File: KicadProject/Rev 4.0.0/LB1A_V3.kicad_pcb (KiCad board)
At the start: 6 copper layers, 42 x 42 mm, 187 parts, among them J601 2337019-1, J602 2337019-1, U101 STM32MP157CAA3, U201 AS4C256M16D3LC-12BCN, U401 STPMIC1xPQR, U501 S40FC004C1B2C00000, U601 LBEE59B1LV-278, U701 DF40C-70DP-0.4V(51), U702 DF40C-100DP-0.4V(51), U703 DF40C-100DP-0.4V(51), X101 32.768kHz, Y101 24MHz

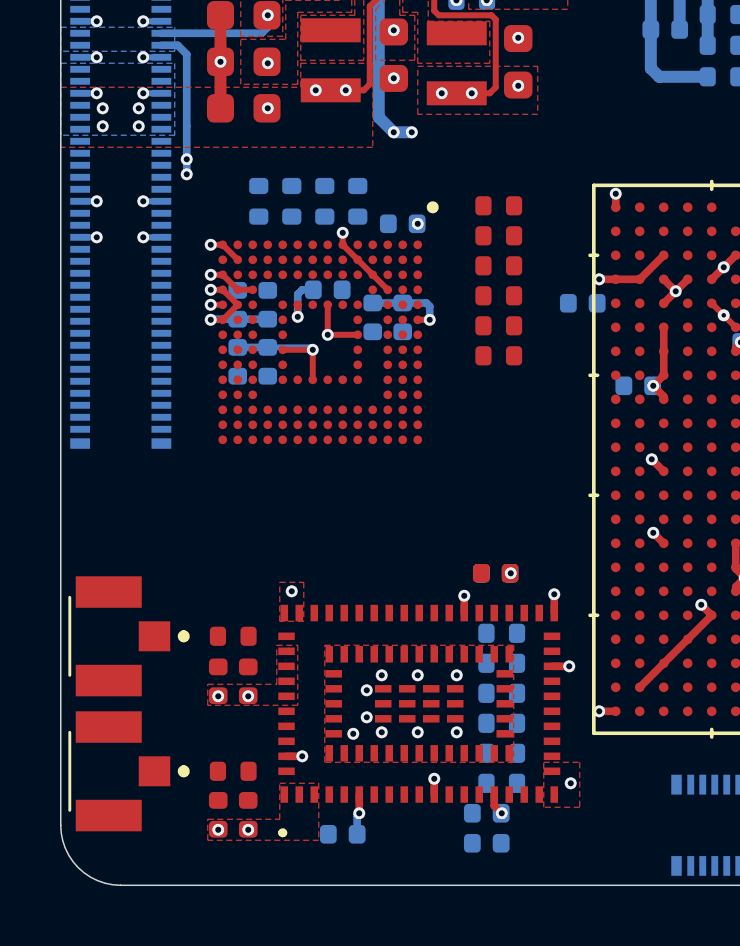
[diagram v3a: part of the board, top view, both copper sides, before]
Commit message: power planes complete.
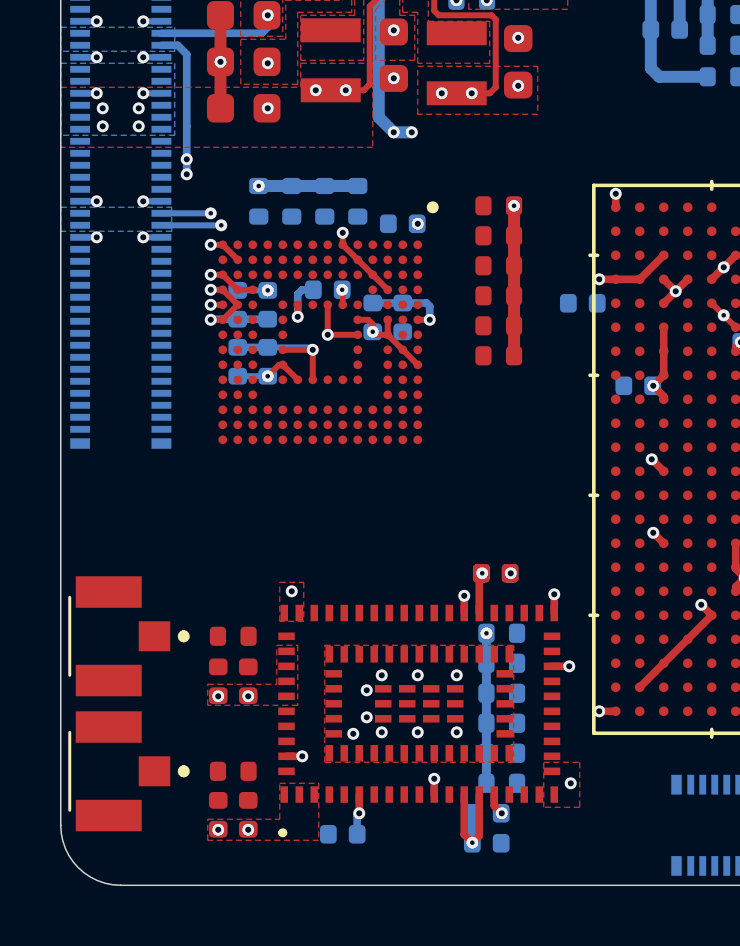
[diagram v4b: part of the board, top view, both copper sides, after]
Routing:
- net PMIC_LDO5_2V9: track 12.7 -> 31.8 mm, vias 5 -> 13
- net PMIC_LDO1_1V8: track 9.00 -> 19.8 mm, vias 3 -> 6
- added copper zone on B.Cu, net PMIC_LDO5_2V9
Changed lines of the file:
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@@
     (thickness 1.2)
     (drawings 8)
-    (tracks 814)
+    (tracks 871)
     (zones 0)
     (modules 187)
@@
   )
   (setup
-    (last_trace_width 0.2)
+    (last_trace_width 0.3)
     (user_trace_width 0.1)
     (user_trace_width 0.127)
@@
   (gr_arc (start 173 128) (end 171 128) (angle -90) (layer Edge.Cuts) (width 0.05))
   (gr_arc (start 173 90) (end 173 88) (angle -90) (layer Edge.Cuts) (width 0.05))
+  (via (at 185.05 119.6) (size 0.4) (drill 0.15) (layers L1_Sig_Pwr.Cu L6_Sig_Pwr.Cu) (net 21))
   (via (at 207.05 110) (size 0.4) (drill 0.15) (layers L1_Sig_Pwr.Cu L6_Sig_Pwr.Cu) (net 9))
   (via (at 201.2 97.4) (size 0.4) (drill 0.15) (layers L1_Sig_Pwr.Cu L6_Sig_Pwr.Cu) (net 9))
@@
   (via (at 175.2 106.3) (size 0.4) (drill 0.2) (layers L1_Sig_Pwr.Cu L6_Sig_Pwr.Cu) (net 21))
   (segment (start 175.2 105.8) (end 175.2 106.3) (width 0.254) (layer L6_Sig_Pwr.Cu) (net 21))
+  (segment (start 185.19 123.6) (end 185.19 123.6) (width 0.4) (layer L6_Sig_Pwr.Cu) (net 21))
+  (segment (start 185.19 123.6) (end 185.19 122.6) (width 0.3) (layer L6_Sig_Pwr.Cu) (net 21))
+  (segment (start 185.19 125.6) (end 185.19 124.6) (width 0.3) (layer L6_Sig_Pwr.Cu) (net 21))
+  (segment (start 185.19 124.6) (end 185.19 124.6) (width 0.4) (layer L6_Sig_Pwr.Cu) (net 21))
+  (segment (start 185.19 125.6) (end 185.19 126.6) (width 0.3) (layer L6_Sig_Pwr.Cu) (net 21))
+  (segment (start 184.72 127.6) (end 184.72 128.58) (width 0.3) (layer L6_Sig_Pwr.Cu) (net 21))
+  (segment (start 184.72 128.58) (end 184.72 128.6) (width 0.4) (layer L6_Sig_Pwr.Cu) (net 21))
+  (via (at 184.72 128.58) (size 0.4) (drill 0.15) (layers L1_Sig_Pwr.Cu L6_Sig_Pwr.Cu) (net 21))
+  (segment (start 184.45 128.31) (end 184.72 128.58) (width 0.254) (layer L1_Sig_Pwr.Cu) (net 21))
+  (segment (start 184.45 126.975) (end 184.45 128.31) (width 0.254) (layer L1_Sig_Pwr.Cu) (net 21))
+  (segment (start 184.95 128.35) (end 184.72 128.58) (width 0.254) (layer L1_Sig_Pwr.Cu) (net 21))
+  (segment (start 184.95 126.975) (end 184.95 128.35) (width 0.254) (layer L1_Sig_Pwr.Cu) (net 21))
+  (segment (start 184.95 119.7) (end 185.05 119.6) (width 0.254) (layer L1_Sig_Pwr.Cu) (net 21))
+  (segment (start 184.95 120.925) (end 184.95 119.7) (width 0.254) (layer L1_Sig_Pwr.Cu) (net 21))
+  (segment (start 185.19 122.6) (end 185.19 121.6) (width 0.3) (layer L6_Sig_Pwr.Cu) (net 21))
+  (segment (start 185.19 121.6) (end 185.19 121.6) (width 0.3) (layer L6_Sig_Pwr.Cu) (net 21))
+  (via (at 185.19 121.6) (size 0.4) (drill 0.15) (layers L1_Sig_Pwr.Cu L6_Sig_Pwr.Cu) (net 21))
+  (segment (start 185.19 124.6) (end 185.19 123.6) (width 0.3) (layer L6_Sig_Pwr.Cu) (net 21))
   (segment (start 177.875 99.45) (end 177.85 99.45) (width 0.254) (layer L1_Sig_Pwr.Cu) (net 22))
   (via (at 175.6 100.2) (size 0.4) (drill 0.2) (layers L1_Sig_Pwr.Cu L6_Sig_Pwr.Cu) (net 22))
@@
   (via (at 176 110.65) (size 0.4) (drill 0.2) (layers L1_Sig_Pwr.Cu L6_Sig_Pwr.Cu) (net 24))
   (segment (start 176.4 110.65) (end 176 110.65) (width 0.2) (layer L1_Sig_Pwr.Cu) (net 24))
+  (segment (start 186.11 112.35) (end 186.11 111.35) (width 0.4) (layer L1_Sig_Pwr.Cu) (net 24))
+  (segment (start 186.11 111.35) (end 186.11 110.35) (width 0.4) (layer L1_Sig_Pwr.Cu) (net 24))
+  (segment (start 186.11 110.35) (end 186.11 109.35) (width 0.4) (layer L1_Sig_Pwr.Cu) (net 24))
+  (segment (start 186.11 109.35) (end 186.11 108.35) (width 0.4) (layer L1_Sig_Pwr.Cu) (net 24))
+  (segment (start 186.11 108.35) (end 186.11 108.11) (width 0.4) (layer L1_Sig_Pwr.Cu) (net 24))
+  (segment (start 186.11 108.11) (end 186.11 107.35) (width 0.4) (layer L1_Sig_Pwr.Cu) (net 24))
+  (segment (start 186.11 107.35) (end 186.11 107.35) (width 0.4) (layer L1_Sig_Pwr.Cu) (net 24))
+  (via (at 186.11 107.35) (size 0.4) (drill 0.15) (layers L1_Sig_Pwr.Cu L6_Sig_Pwr.Cu) (net 24))
+  (segment (start 180.9 106.69) (end 179.8 106.69) (width 0.4) (layer L6_Sig_Pwr.Cu) (net 24))
+  (segment (start 179.8 106.69) (end 178.7 106.69) (width 0.4) (layer L6_Sig_Pwr.Cu) (net 24))
+  (segment (start 178.7 106.69) (end 177.6 106.69) (width 0.4) (layer L6_Sig_Pwr.Cu) (net 24))
+  (segment (start 177.6 106.69) (end 177.6 106.69) (width 0.4) (layer L6_Sig_Pwr.Cu) (net 24))
+  (via (at 177.6 106.69) (size 0.4) (drill 0.15) (layers L1_Sig_Pwr.Cu L6_Sig_Pwr.Cu) (net 24))
+  (via (at 180.38 110.15) (size 0.4) (drill 0.15) (layers L1_Sig_Pwr.Cu L6_Sig_Pwr.Cu) (net 24))
+  (segment (start 180.4 110.17) (end 180.38 110.15) (width 0.2) (layer L1_Sig_Pwr.Cu) (net 24))
+  (segment (start 180.4 110.65) (end 180.4 110.17) (width 0.2) (layer L1_Sig_Pwr.Cu) (net 24))
+  (segment (start 180.9 111.15) (end 181.25 111.15) (width 0.2) (layer L1_Sig_Pwr.Cu) (net 24))
+  (via (at 181.4 111.55) (size 0.4) (drill 0.15) (layers L1_Sig_Pwr.Cu L6_Sig_Pwr.Cu) (net 24))
+  (segment (start 181.4 111.3) (end 181.4 111.55) (width 0.2) (layer L1_Sig_Pwr.Cu) (net 24))
+  (segment (start 181.25 111.15) (end 181.4 111.3) (width 0.2) (layer L1_Sig_Pwr.Cu) (net 24))
+  (segment (start 181.9 111.15) (end 181.9 111.65) (width 0.2) (layer L1_Sig_Pwr.Cu) (net 24))
+  (segment (start 181.9 111.65) (end 182.4 112.15) (width 0.2) (layer L1_Sig_Pwr.Cu) (net 24))
+  (segment (start 182.4 112.15) (end 182.9 112.65) (width 0.2) (layer L1_Sig_Pwr.Cu) (net 24))
+  (segment (start 181.5 111.65) (end 181.4 111.55) (width 0.2) (layer L1_Sig_Pwr.Cu) (net 24))
+  (segment (start 181.9 111.65) (end 181.5 111.65) (width 0.2) (layer L1_Sig_Pwr.Cu) (net 24))
+  (segment (start 178.9 113.15) (end 178.4 112.65) (width 0.2) (layer L1_Sig_Pwr.Cu) (net 24))
+  (via (at 177.9 113.03) (size 0.4) (drill 0.15) (layers L1_Sig_Pwr.Cu L6_Sig_Pwr.Cu) (net 24))
+  (segment (start 178.28 112.65) (end 177.9 113.03) (width 0.2) (layer L1_Sig_Pwr.Cu) (net 24))
+  (segment (start 178.4 112.65) (end 178.28 112.65) (width 0.2) (layer L1_Sig_Pwr.Cu) (net 24))
+  (segment (start 176.9 113.03) (end 177.9 113.03) (width 0.2) (layer L6_Sig_Pwr.Cu) (net 24))
+  (segment (start 176.9 110.17) (end 177.9 110.17) (width 0.2) (layer L6_Sig_Pwr.Cu) (net 24))
+  (segment (start 177.9 110.17) (end 177.9 110.17) (width 0.2) (layer L6_Sig_Pwr.Cu) (net 24))
+  (via (at 177.9 110.17) (size 0.4) (drill 0.15) (layers L1_Sig_Pwr.Cu L6_Sig_Pwr.Cu) (net 24))
+  (via (at 176 107.6) (size 0.4) (drill 0.15) (layers L1_Sig_Pwr.Cu L6_Sig_Pwr.Cu) (net 24))
+  (segment (start 174.355 107.6) (end 176 107.6) (width 0.2) (layer L6_Sig_Pwr.Cu) (net 24))
+  (segment (start 174.355 108) (end 174.45 108) (width 0.2) (layer L6_Sig_Pwr.Cu) (net 24))
+  (via (at 176.35 108) (size 0.4) (drill 0.15) (layers L1_Sig_Pwr.Cu L6_Sig_Pwr.Cu) (net 24))
+  (segment (start 174.45 108) (end 176.35 108) (width 0.2) (layer L6_Sig_Pwr.Cu) (net 24))
   (segment (start 183.35 94.75) (end 183.35 93.95) (width 0.127) (layer L1_Sig_Pwr.Cu) (net 35))
   (segment (start 183.35 93.95) (end 183.60402 93.69598) (width 0.127) (layer L1_Sig_Pwr.Cu) (net 35))
@@
       )
     )
+  )
+  (zone (net 24) (net_name PMIC_LDO5_2V9) (layer L6_Sig_Pwr.Cu) (hatch none 0.508)
+    (connect_pads yes (clearance 0.1))
+    (min_thickness 0.1)
+    (fill yes (arc_segments 32) (thermal_gap 0.508) (thermal_bridge_width 0.508))
+    (polygon
+      (pts
+        (xy 174.7 108.2) (xy 171 108.2) (xy 171 107.4) (xy 174.7 107.4)
+      )
+    )

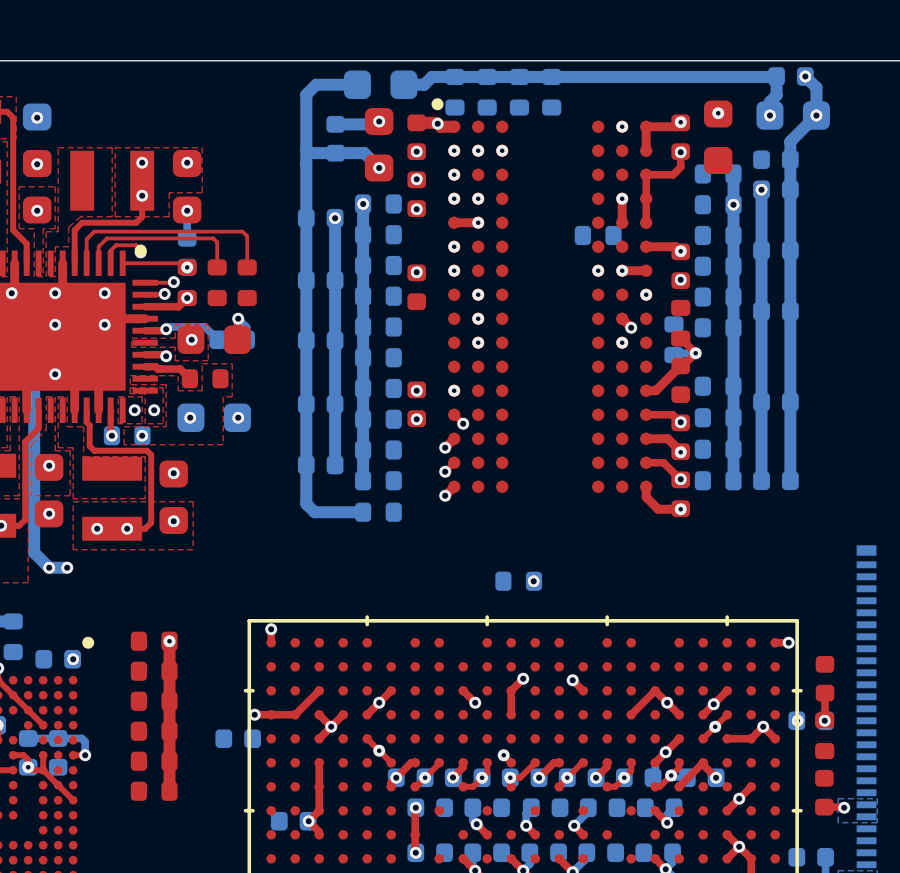
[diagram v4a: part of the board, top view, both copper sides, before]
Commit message: started ddr3 routing
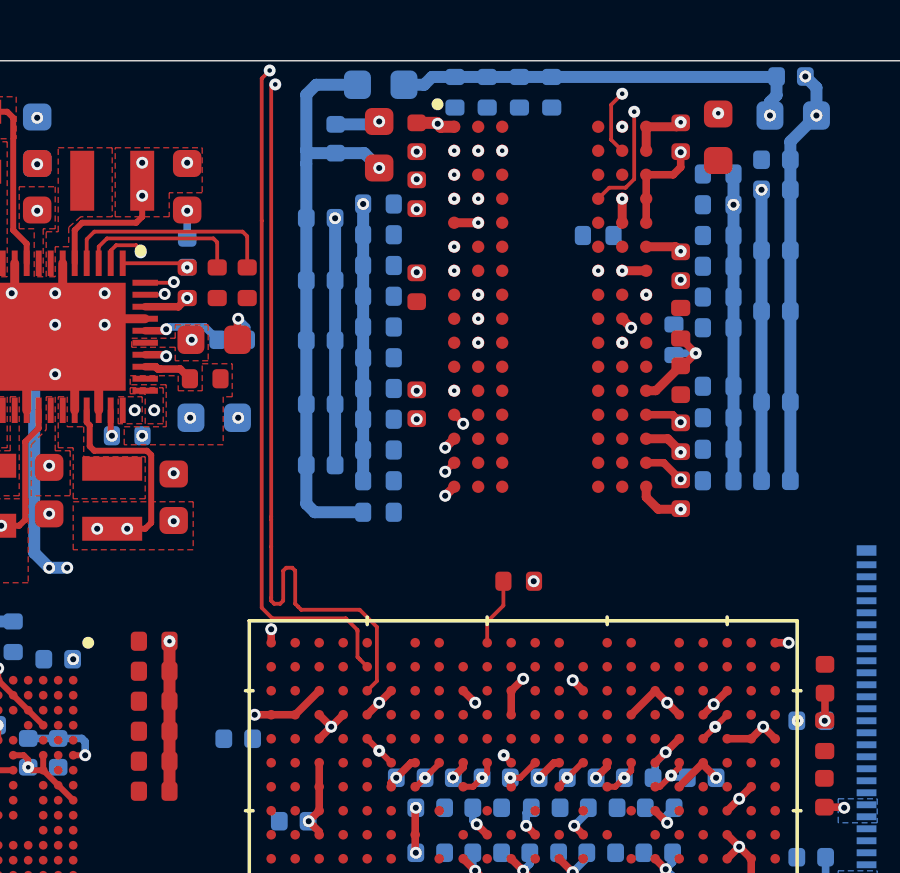
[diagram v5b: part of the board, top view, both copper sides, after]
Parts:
- R210: moved to F.Cu
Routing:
- net /MPU_DDR3L_Memory/DDR_DQ0: track 0.00 -> 40.0 mm, vias 0 -> 2
- net /MPU_DDR3L_Memory/DDR_DQ3: track 0.00 -> 40.0 mm, vias 0 -> 2
- net Net-(R210-Pad1): track 0.00 -> 2.27 mm

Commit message: working on ddr3 routing
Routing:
- net /MPU_DDR3L_Memory/DDR_DQ7: track 0.00 -> 40.1 mm, vias 0 -> 2
- net /MPU_DDR3L_Memory/DDR_DQ1: track 0.00 -> 39.9 mm, vias 0 -> 2

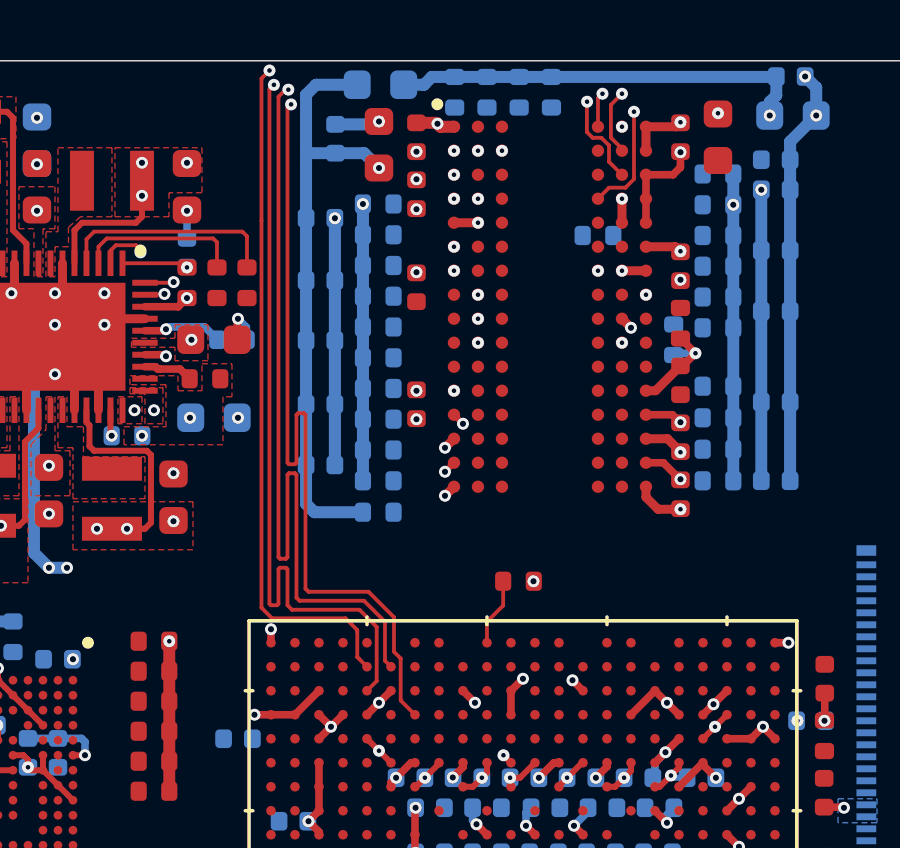
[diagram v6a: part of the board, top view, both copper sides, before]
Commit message: routed another ddr3 track
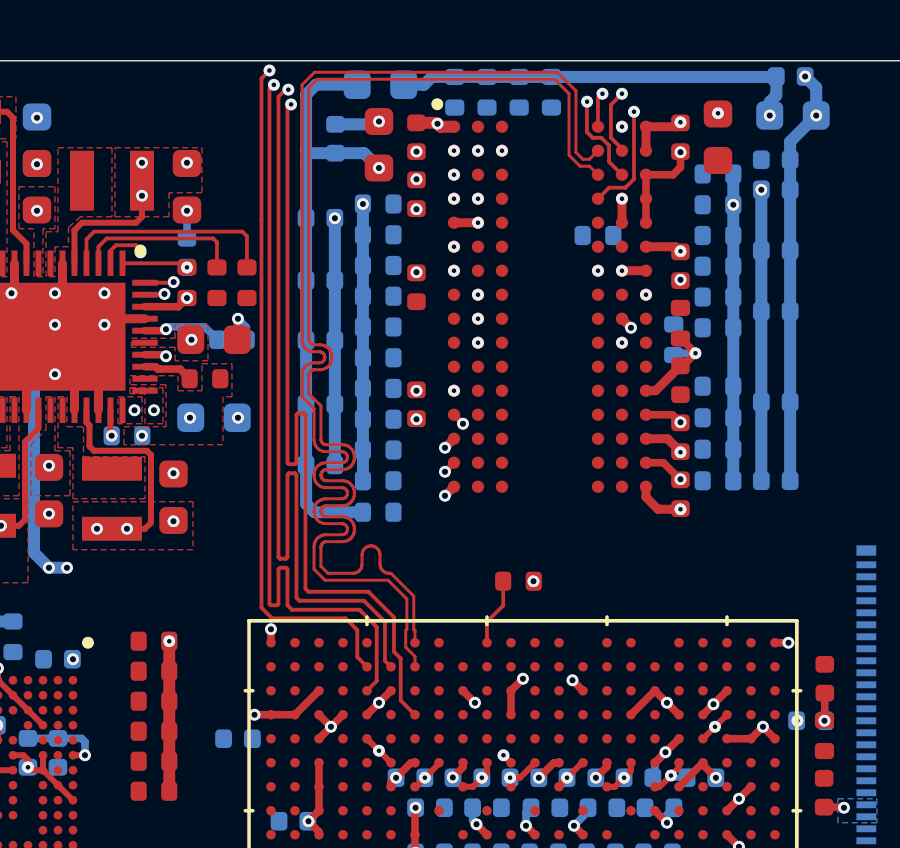
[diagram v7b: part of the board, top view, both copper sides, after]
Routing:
- net /MPU_DDR3L_Memory/DDR_DQS0_P: track 0.00 -> 41.0 mm
- net /MPU_DDR3L_Memory/DDR_DQS0_N: track 0.00 -> 41.0 mm

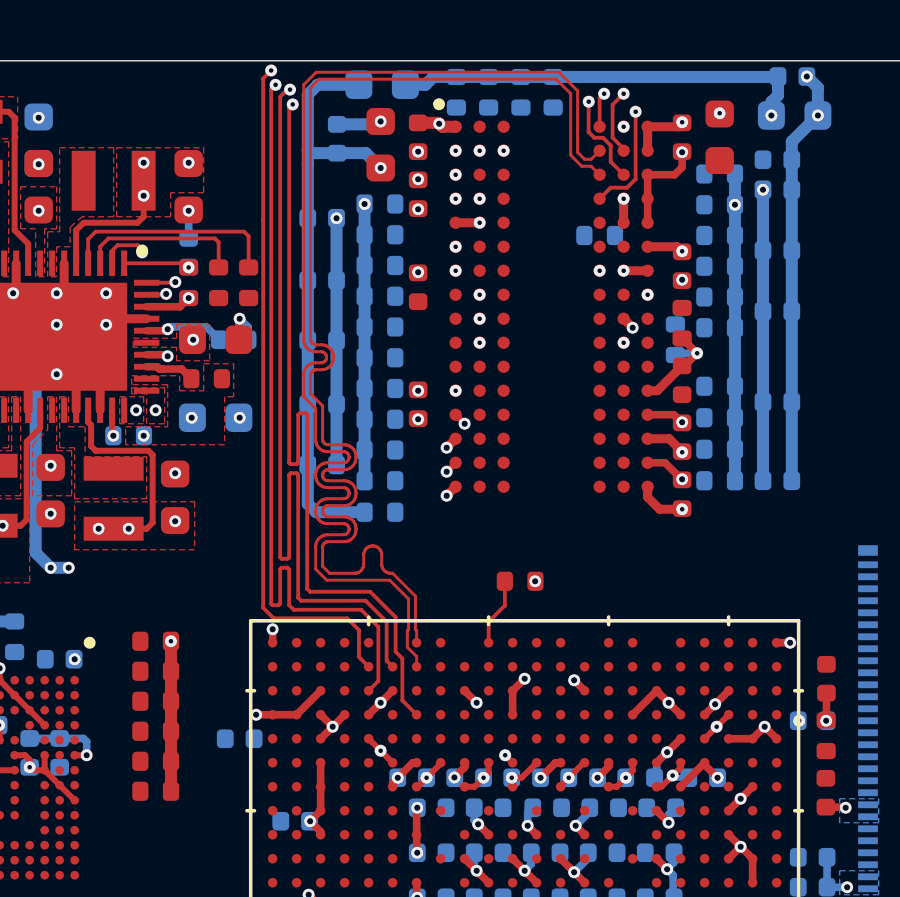
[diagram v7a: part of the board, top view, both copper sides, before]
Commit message: rerouting ddr3 tracks
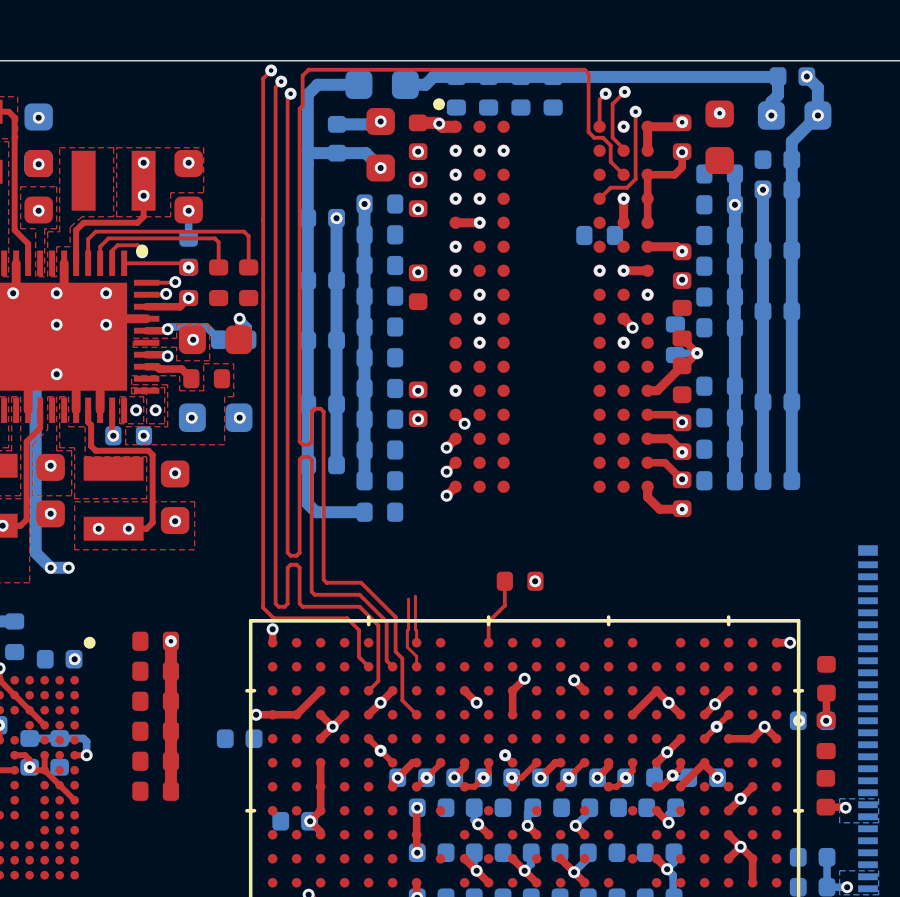
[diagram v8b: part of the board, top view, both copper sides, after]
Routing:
- net /MPU_DDR3L_Memory/DDR_DQS0_P: track 41.0 -> 1.57 mm
- net /MPU_DDR3L_Memory/DDR_DQS0_N: track 41.0 -> 2.40 mm
- net /MPU_DDR3L_Memory/DDR_DQ7: track 40.1 -> 40.0 mm, vias 2 -> 0
